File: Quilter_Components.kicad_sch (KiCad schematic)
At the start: 38 parts, among them J1 Conn_01x10_Male, J2 Conn_01x10_Male, J3 Conn_01x10_Male, J4 Eurorack_10_pin_power, U1 TL072, U2 TL074, U3 TL074, U4 TL074

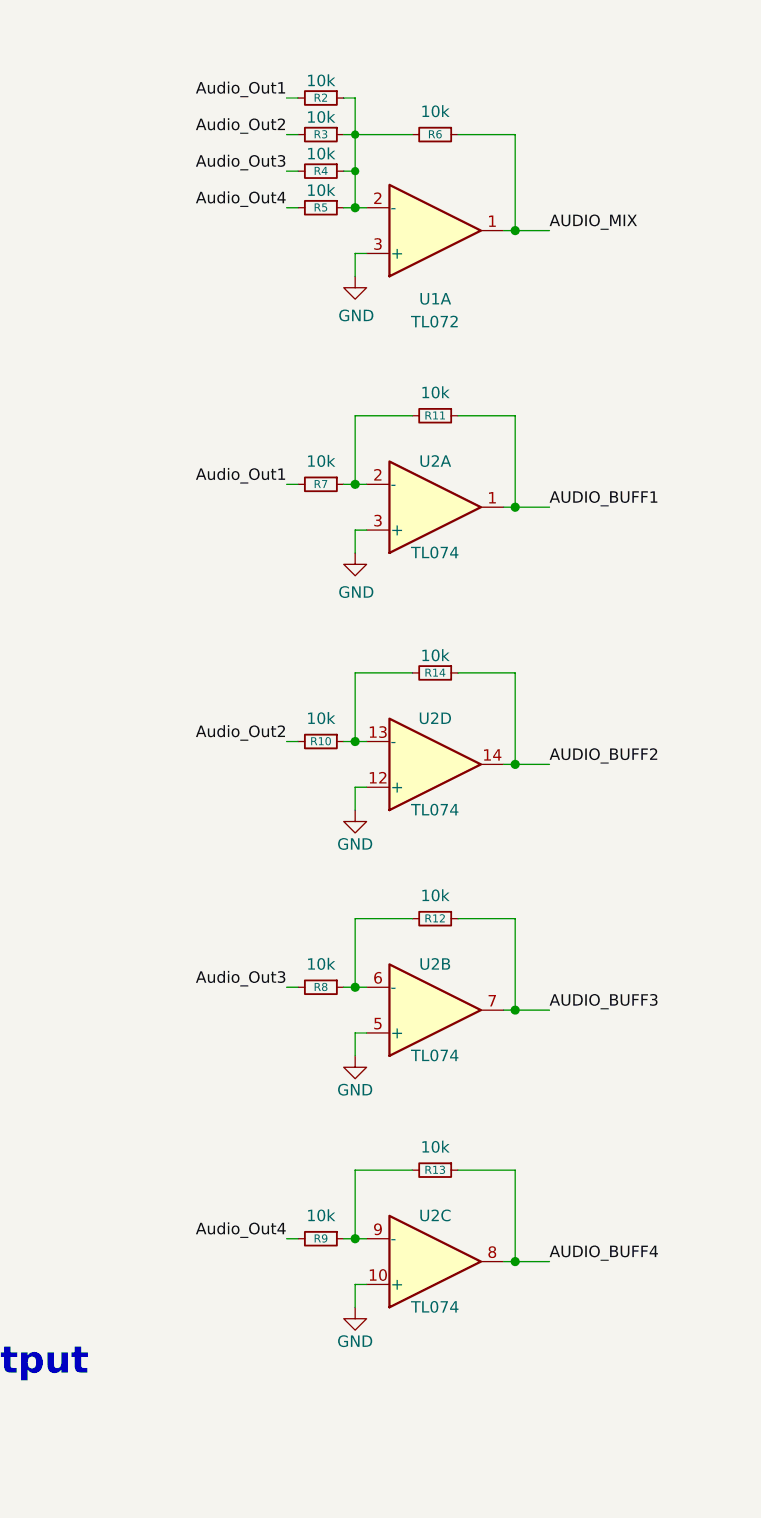
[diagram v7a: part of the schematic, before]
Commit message: Added op-amp output protection resistors
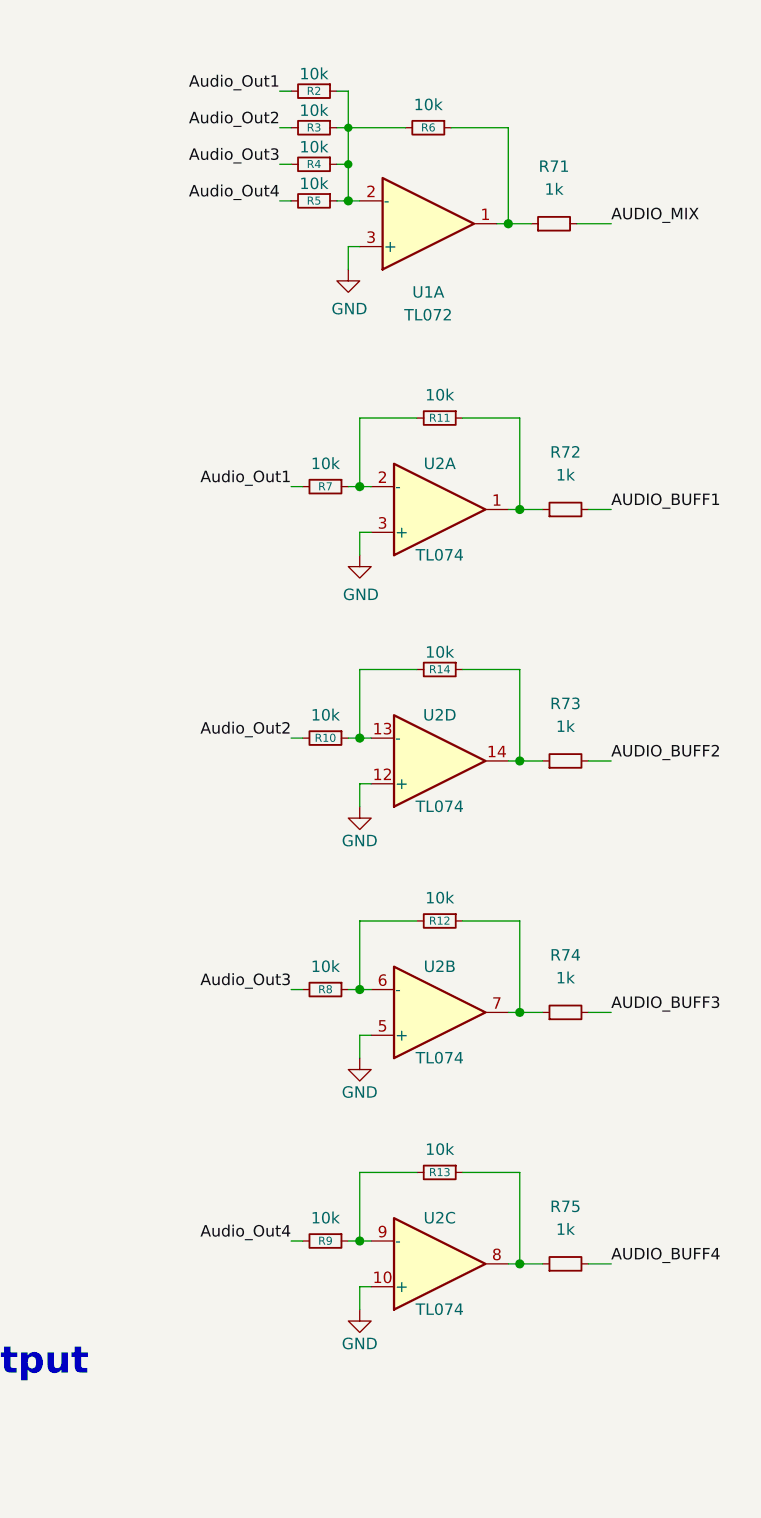
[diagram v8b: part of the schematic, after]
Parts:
- added R71, R72, R73, R74, R75: 1k, Resistor_SMD:R_0603_1608Metric_Pad0.98x0.95mm_HandSolder, symbol Device:R_Small
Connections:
- net AUDIO_BUFF1: now also R72.2; no longer R11.1, U2.1
- net AUDIO_BUFF2: now also R73.2; no longer R14.1, U2.14
- net AUDIO_BUFF3: now also R74.2; no longer R12.1, U2.7
- net AUDIO_BUFF4: now also R75.2; no longer R13.1, U2.8
- net AUDIO_MIX: now also R71.2; no longer R6.1, U1.1
- new net: R6.1, R71.1, U1.1
- new net: R12.1, R74.1, U2.7
- new net: R14.1, R73.1, U2.14
- new net: R11.1, R72.1, U2.1
- new net: R13.1, R75.1, U2.8
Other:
- moved on the sheet: R10, R11, R12, R13, R14, R2, R3, R4, R5, R6, R7, R8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
